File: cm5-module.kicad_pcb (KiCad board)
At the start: 4 copper layers, 100 x 100 mm, 181 parts, among them J1 DIN-41612-connector_090319679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, J10 MicroSD_5033981892, J11 JST_SH_1x4_BM04B-SRSS-TB-LF-SN, J2 CM5_1-100_3mm-stack, J3 CM5_101-200_3mm-stack, J4 JST_SH_1x3_BM03B-SRSS-TB-LF-SN, J5 Bus_M.2_1-2199230-6, J6 RJ45_HC612601A-M893-A, J7 USB-A_USB-303WSD-BRY, J8 HDMI-A_HDMI-19PIN-043, J9 USB-C_USB-310F-B-SU, Q1 SIS472DN-T1-GE3, Q2 SIS472DN-T1-GE3, Q3 AO3400A, Q4 SIS472DN-T1-GE3, SW1 SW_TL2243, U1 AP22615AWU-7, U10 AP22615AWU-7, U11 AP22615AWU-7, U12 LM74700QDBVRQ1, U2 AP22615AWU-7, U3 FT230XQ-R, U4 NTS0102DP, U5 CH334P, U6 LM74700QDBVRQ1, U7 SIC431AED-T1-GE3, U8 LM74700QDBVRQ1, U9 TPS564247DRLR, Y1 Oscillator_32.768kHz_OK2EL89C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, Y2 X322512MSB4SI

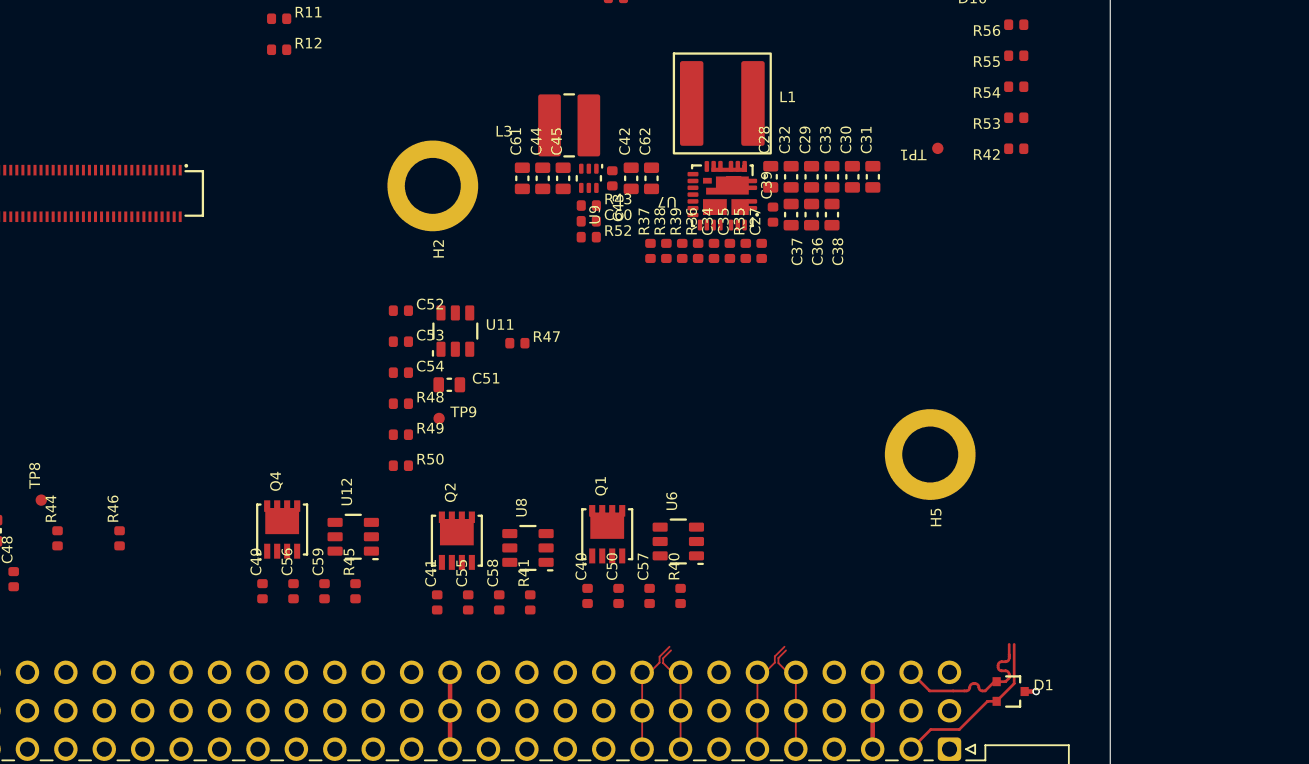
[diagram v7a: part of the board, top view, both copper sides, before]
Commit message: [#1] Add USB to CAN schematic, add power flags to 5V and 3V3
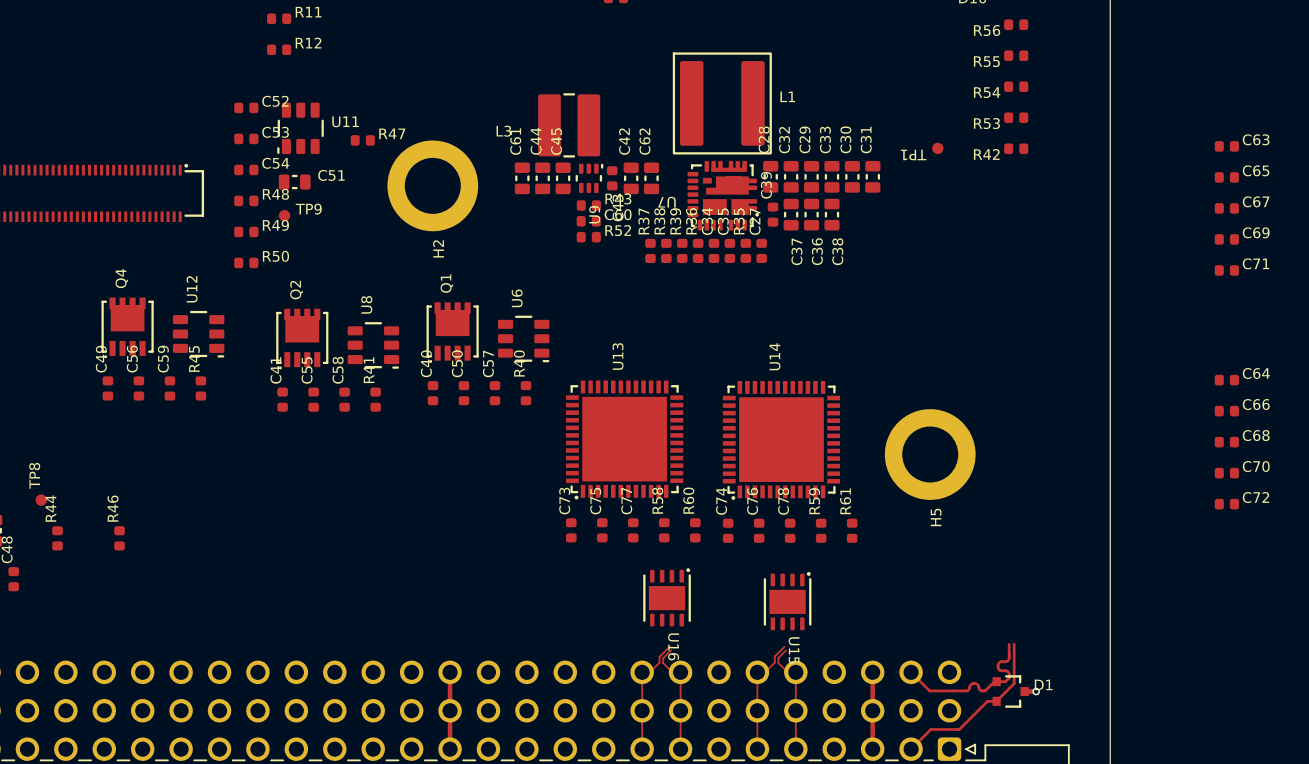
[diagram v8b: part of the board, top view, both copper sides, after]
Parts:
- added C63: C-100n-0402, DW-footprints:C_0402_1005Metric, F.Cu at (147.1, 106.1)
- added C64: C-100n-0402, DW-footprints:C_0402_1005Metric, F.Cu at (147.1, 121.6)
- added C65: C-100n-0402, DW-footprints:C_0402_1005Metric, F.Cu at (147.1, 108.2)
- added C66: C-100n-0402, DW-footprints:C_0402_1005Metric, F.Cu at (147.1, 123.6)
- added C67: C-100n-0402, DW-footprints:C_0402_1005Metric, F.Cu at (147.1, 110.2)
- added C68: C-100n-0402, DW-footprints:C_0402_1005Metric, F.Cu at (147.1, 125.7)
- added C69: C-100n-0402, DW-footprints:C_0402_1005Metric, F.Cu at (147.1, 112.3)
- added C70: C-100n-0402, DW-footprints:C_0402_1005Metric, F.Cu at (147.1, 127.7)
- added C71: C-100n-0402, DW-footprints:C_0402_1005Metric, F.Cu at (147.1, 114.3)
- added C72: C-100n-0402, DW-footprints:C_0402_1005Metric, F.Cu at (147.1, 129.8)
- added C73: C-100n-0402, DW-footprints:C_0402_1005Metric, F.Cu at (103.7, 131.5)
- added C74: C-100n-0402, DW-footprints:C_0402_1005Metric, F.Cu at (114.1, 131.5)
- added C75: C-100n-0402, DW-footprints:C_0402_1005Metric, F.Cu at (105.8, 131.5)
- added C76: C-100n-0402, DW-footprints:C_0402_1005Metric, F.Cu at (116.2, 131.5)
- added C77: C-100n-0402, DW-footprints:C_0402_1005Metric, F.Cu at (107.8, 131.5)
- added C78: C-100n-0402, DW-footprints:C_0402_1005Metric, F.Cu at (118.2, 131.5)
- added R58: R-10k-0402, DW-footprints:R_0402_1005Metric, F.Cu at (109.9, 131.5)
- added R59: R-10k-0402, DW-footprints:R_0402_1005Metric, F.Cu at (120.3, 131.5)
- added R60: R-10k-0402, DW-footprints:R_0402_1005Metric, F.Cu at (111.9, 131.5)
- added R61: R-10k-0402, DW-footprints:R_0402_1005Metric, F.Cu at (122.3, 131.5)
- added U13: STM32G431CBU6, DW-footprints:UFQFPN-48-1EP_7x7mm_P0.5mm_EP5.7x5.7mm, F.Cu at (107.3, 125.5)
- added U14: STM32G431CBU6, DW-footprints:UFQFPN-48-1EP_7x7mm_P0.5mm_EP5.7x5.7mm, F.Cu at (117.6, 125.5)
- added U15: TJA1044GTK_3Z, DW-footprints:HVSON-8-1EP_3x3mm_P0.65mm_EP1.6x2.4mm, F.Cu at (118.0, 136.2)
- added U16: TJA1044GTK_3Z, DW-footprints:HVSON-8-1EP_3x3mm_P0.65mm_EP1.6x2.4mm, F.Cu at (110.1, 136.0)
- moved C49 16.9 mm to (73.1, 122.1)
- moved C56 16.9 mm to (75.2, 122.1)
- moved C59 16.9 mm to (77.2, 122.1)
- moved R45 16.9 mm to (79.2, 122.1)
- moved C40 16.9 mm to (94.6, 122.4)
- moved C50 16.9 mm to (96.6, 122.4)
- moved C51 16.9 mm to (85.5, 108.5)
- moved C52 16.9 mm to (82.2, 103.6)
- moved C53 16.9 mm to (82.2, 105.6)
- moved C54 16.9 mm to (82.2, 107.7)
- moved C57 16.9 mm to (98.7, 122.4)
- moved Q2 16.9 mm to (86.0, 118.8)
- moved Q4 16.9 mm to (74.4, 118.0)
- moved R40 16.9 mm to (100.7, 122.4)
- moved R47 16.9 mm to (90.0, 105.7)
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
